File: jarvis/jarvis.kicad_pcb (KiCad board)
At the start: 4 copper layers, 17.5 x 45.8 mm, 30 parts, among them IC1 ESP32-S3R16V, IC2 MAX98357AETE+T, IC3 MCP73871T-4CAI_ML, IC4 TLV70033DDCT, J1 Conn_01x02 - Speaker, J2 Mic Conn_01x05, J3 Conn_01x02 - Battery, U1 W25Q64JVSSIQ, U2 2137160001, Y1 Crystal 32.768khz, Y2 Crystal 40mhz

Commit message: flash routed
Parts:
- removed PESD5: PESD5V0X1UAB,115, jarvis:PESD5V0X1UAB115
- removed U1: W25Q64JVSSIQ, jarvis:W25Q64JVSSIQ
- added AE1: RFANT3216120A5T, jarvis:ANT_RFANT3216120A5T_WAL, F.Cu at (146.1, 92.9)
- added C11: 0.1uf, Capacitor_SMD:C_0603_1608Metric, F.Cu at (72.5, 48.4)
- added C12: 0.1uf, Capacitor_SMD:C_0603_1608Metric, F.Cu at (72.5, 51.0)
- added C13: 0.1uf, Capacitor_SMD:C_0603_1608Metric, F.Cu at (76.5, 43.4)
- added C14: 12pf, Capacitor_SMD:C_0402_1005Metric, F.Cu at (82.0, 57.1)
- added C15: 0.1uf, Capacitor_SMD:C_0603_1608Metric, F.Cu at (76.5, 45.9)
- added C16: 12pf, Capacitor_SMD:C_0402_1005Metric, F.Cu at (82.0, 59.1)
- added C17: 1uf, Capacitor_SMD:C_0603_1608Metric, F.Cu at (76.5, 48.4)
- added C18: 0.1uf, Capacitor_SMD:C_0402_1005Metric, F.Cu at (82.0, 61.1)
- added C19: 0.1uf, Capacitor_SMD:C_0603_1608Metric, F.Cu at (76.5, 51.0)
- added C20: 10uf, Capacitor_SMD:C_0603_1608Metric, F.Cu at (80.6, 43.4)
- added C21: 1uf, Capacitor_SMD:C_0603_1608Metric, F.Cu at (80.6, 45.9)
- added IC5: W25Q128JWSIQ, jarvis:W25Q128JWSIQ-1.8, F.Cu at (165.7, 111.7)
- added L2: 24nh, jarvis:MLG1005SR24JT000, F.Cu at (75.9, 60.7)
- added L3: 6.8 nH, Inductor_SMD:L_01005_0402Metric, F.Cu at (147.8, 97.9)
- added PESD1: PESD5V0X1UAB,115, jarvis:PESD5V0X1UAB115, F.Cu at (62.8, 60.3)
- added R10: 0, Resistor_SMD:R_0603_1608Metric, F.Cu at (156.8, 112.4)
- added R11: 0, Resistor_SMD:R_0603_1608Metric, F.Cu at (156.8, 110.9)
- added R12: 0, Resistor_SMD:R_0603_1608Metric, F.Cu at (156.8, 109.3)
- added R13: 0, Resistor_SMD:R_0603_1608Metric, F.Cu at (156.8, 107.8)
- added R14: 0, Resistor_SMD:R_0603_1608Metric, F.Cu at (156.8, 113.9)
- added R15: 0, Resistor_SMD:R_0603_1608Metric, F.Cu at (156.8, 115.5)
- added R8: 10k, Resistor_SMD:R_0603_1608Metric, F.Cu at (80.6, 51.0)
- added R9: 10k, Resistor_SMD:R_0603_1608Metric, F.Cu at (153.8, 100.6)
- added S1: EVQ-P9H02W, jarvis:EVQP9H02W, F.Cu at (87.4, 57.1)
- C1: value 1uf -> 10uf
- C10, C9: footprint Capacitor_SMD:C_0603_1608Metric -> Capacitor_SMD:C_0402_1005Metric
- C2: value 10uf -> 4.7uf
- C3: value 4.7uf -> 1uf
- C7, C8: value 12pf -> 0.1uf
- IC1, IC2, IC3: moved to F.Cu
- R1: value 2k -> 10k
- R2: value 10k -> 2k
- R4: value 5.1k -> 22
- R6: value 22 -> 5.1k
- moved U2 120.3 mm to (53.7, 45.2), turned to 0 degrees
- moved R3 118.0 mm to (58.8, 55.3), turned to 0 degrees
- moved R4 114.8 mm to (58.8, 57.8), turned to 0 degrees
- moved C3 106.2 mm to (50.8, 60.4), turned to 0 degrees
- moved IC3 105.0 mm to (65.6, 45.1), turned to 0 degrees
- moved C1 104.7 mm to (50.8, 55.3), turned to 0 degrees
- moved C5 103.5 mm to (54.8, 55.3), turned to 0 degrees
- moved R2 102.8 mm to (54.8, 62.9), turned to 0 degrees
- moved R7 101.5 mm to (80.6, 48.4), turned to 0 degrees
- moved IC4 101.4 mm to (65.0, 50.1)
- moved J3 101.3 mm to (63.4, 57.1)
- moved C4 100.8 mm to (50.8, 62.9), turned to 0 degrees
- moved C2 100.6 mm to (50.8, 57.8), turned to 0 degrees
- moved C9 99.8 mm to (82.0, 53.2)
- moved C6 99.6 mm to (54.8, 57.8), turned to 0 degrees
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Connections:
- net Net-(IC1-GPIO18) renamed /ESP/ESP-GPIO17
- net Net-(IC1-GPIO3) renamed /Components/AMP-DIN
- C1 pad 1: VBUS -> /Power/VBAT_1
- C10 pad 1: Net-(IC1-XTAL_32K_P) -> Net-(IC1-XTAL_32K_N)
- C2 pad 1: /VBAT_1 -> GND
- C2 pad 2: GND -> /Power/SYS
- C3 pad 1: GND -> VBUS
- C3 pad 2: /SYS -> GND
- C4 pad 2: /SYS -> /Power/SYS
- C7 pad 1: Net-(IC1-XTAL_N) -> +3.3V
- C8 pad 1: GND -> +3.3V
- C8 pad 2: Net-(C8-Pad2) -> GND
- C9 pad 1: Net-(IC1-XTAL_32K_N) -> Net-(IC1-XTAL_32K_P)
- IC1 pad 1: unconnected-(IC1-LNA_IN-Pad1) -> Net-(IC1-LNA_IN)
- IC1 pad 10: Net-(IC1-GPIO5) -> /Components/AMP-BCLK
- IC1 pad 12: unconnected-(IC1-GPIO7-Pad12) -> /Components/MIC-WS
- IC1 pad 13: unconnected-(IC1-GPIO8-Pad13) -> /Components/MIC-BCK
- IC1 pad 14: unconnected-(IC1-GPIO9-Pad14) -> /Components/MIC-DATA
- IC1 pad 2: unconnected-(IC1-VDD3P3_1-Pad2) -> Net-(IC1-VDD3P3_1)
- IC1 pad 20: unconnected-(IC1-VDD3P3_RTC-Pad20) -> +3.3V
- IC1 pad 23: Net-(IC1-GPIO17) -> /ESP/ESP-GPIO18
- IC1 pad 25: Net-(IC1-GPIO19) -> /ESP/ESP-GPIO19
- IC1 pad 26: Net-(IC1-GPIO20) -> /ESP/ESP-GPIO20
- IC1 pad 27: Net-(IC1-GPIO21) -> /ESP/ESP-GPIO21
- IC1 pad 29: unconnected-(IC1-VDD_SPI-Pad29) -> +1.8
- IC1 pad 3: unconnected-(IC1-VDD3P3_2-Pad3) -> Net-(IC1-VDD3P3_1)
- IC1 pad 30: unconnected-(IC1-SPIHD-Pad30) -> Net-(IC1-SPIHD)
- IC1 pad 31: unconnected-(IC1-SPIWP-Pad31) -> Net-(IC1-SPIWP)
- IC1 pad 32: /SYS -> Net-(IC1-SPICS0)
- IC1 pad 4: unconnected-(IC1-CHIP_PU-Pad4) -> Net-(IC1-CHIP_PU)
- IC1 pad 43: Net-(IC1-GPIO38) -> unconnected-(IC1-GPIO38-Pad43)
- IC1 pad 46: unconnected-(IC1-VDD3P3_CPU-Pad46) -> +3.3V
- IC1 pad 52: Net-(IC1-GPIO46) -> unconnected-(IC1-GPIO46-Pad52)
- IC1 pad 55: unconnected-(IC1-VDDA_1-Pad55) -> +3.3V
- IC1 pad 56: unconnected-(IC1-VDDA_2-Pad56) -> +3.3V
- IC1 pad 9: Net-(IC1-GPIO4) -> /Components/AMP-LRCLK
- IC2 pad 14: Net-(IC1-GPIO5) -> /Components/AMP-LRCLK
- IC2 pad 16: Net-(IC1-GPIO4) -> /Components/AMP-BCLK
- IC2 pad 4: +3.3V -> /Components/+3.3V
- IC2 pad 7: +3.3V -> /Components/+3.3V
- IC2 pad 8: +3.3V -> /Components/+3.3V
- IC3 pad 1: /SYS -> /Power/SYS
- IC3 pad 13: /PROG1 -> /Power/PROG1
- IC3 pad 14: /VBAT_1 -> /Power/VBAT_1
- IC3 pad 17: /VBAT_1 -> /Power/VBAT_1
- IC3 pad 20: /SYS -> /Power/SYS
- IC3 pad 5: /THERM -> /Power/THERM
- IC3 pad 7: Net-(IC1-GPIO17) -> /ESP/ESP-GPIO21
- IC3 pad 8: Net-(IC1-GPIO21) -> /ESP/ESP-GPIO18
- IC4 pad 1: /SYS -> /Power/SYS
- IC4 pad 3: /SYS -> /Power/SYS
- J2 pad 1: Net-(IC1-GPIO38) -> /Components/MIC-DATA
- J2 pad 2: Net-(IC1-GPIO45) -> /Components/MIC-WS
- J2 pad 3: Net-(IC1-GPIO46) -> /Components/MIC-BCK
- J2 pad 4: +3.3V -> /Components/+3.3
- J3 pad 1: /VBAT_1 -> /Power/VBAT_1
- L1 pad 2: Net-(C8-Pad2) -> Net-(C14-Pad2)
- R1 pad 1: /PROG1 -> GND
- R1 pad 2: GND -> /Power/THERM
- R2 pad 1: GND -> /Power/PROG1
- R2 pad 2: /THERM -> GND
- R4 pad 1: GND -> /Power/USB_DP
- R4 pad 2: Net-(U2-CC2) -> /ESP/ESP-GPIO19
- R5 pad 1: /USB_DP -> /Power/USB_DN
- R5 pad 2: Net-(IC1-GPIO19) -> /ESP/ESP-GPIO20
- R6 pad 1: /USB_DN -> GND
- R6 pad 2: Net-(IC1-GPIO20) -> Net-(U2-CC2)
- U2 pad A6: /USB_DP -> /Power/USB_DP
- U2 pad A7: /USB_DN -> /Power/USB_DN
- U2 pad B6: /USB_DP -> /Power/USB_DP
- U2 pad B7: /USB_DN -> /Power/USB_DN
- Y2 pad 2: Net-(C8-Pad2) -> Net-(C14-Pad2)
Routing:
- net GND: track 64.2 -> 1.60 mm, vias 20 -> 1
- net /USB_DN: track 47.8 -> 0.00 mm, vias 1 -> 0
- net /SYS: track 40.2 -> 0.00 mm, vias 2 -> 0
- net VBUS: track 37.4 -> 0.00 mm, vias 3 -> 0
- net +3.3V: track 30.1 -> 0.00 mm, vias 3 -> 0
- net Net-(IC1-XTAL_32K_P): track 27.8 -> 0.00 mm, vias 1 -> 0
- net Net-(IC1-XTAL_32K_N): track 27.6 -> 0.00 mm, vias 1 -> 0
- net Net-(U2-CC2): track 21.6 -> 0.00 mm, vias 1 -> 0
- net Net-(IC1-GPIO17): track 20.4 -> 0.00 mm
- net Net-(IC1-GPIO21): track 19.4 -> 0.00 mm
- net +1.8: track 0.00 -> 19.3 mm, vias 0 -> 2
- net /ESP/ESP-GPIO17: track 18.8 -> 0.00 mm
- net Net-(IC1-GPIO46): track 18.0 -> 0.00 mm
- net /VBAT_1: track 17.3 -> 0.00 mm, vias 1 -> 0
- net Net-(IC1-GPIO45): track 16.4 -> 0.00 mm
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- removed copper zone on In2.Cu, net +3.3V
- removed copper zone on In1.Cu, net GND
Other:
- board outline removed
- board text removed: "Jarvis"

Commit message: start crystal layout
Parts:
- moved IC4 141.1 mm to (184.3, 125.3)
- moved J3 133.2 mm to (169.9, 137.2)
- moved IC3 125.4 mm to (151.7, 136.2)
- moved U2 125.0 mm to (173.6, 80.4)
- moved Y1 96.7 mm to (148.1, 119.2)
- moved J2 94.4 mm to (117.2, 138.7)
- moved Y2 86.7 mm to (149.0, 102.8), turned to 180 degrees
- moved L1 86.1 mm to (148.2, 105.2), turned to 90 degrees
- moved C16 81.3 mm to (151.1, 102.0), turned to 90 degrees
- moved C14 78.5 mm to (146.7, 101.7), turned to -90 degrees
- moved IC2 65.5 mm to (124.0, 122.8)
- moved J1 65.5 mm to (117.6, 123.5)
- moved S1 62.2 mm to (119.6, 110.2)
- moved C8 54.6 mm to (114.8, 80.4)
- moved R1 54.6 mm to (97.1, 94.8)
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
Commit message: crystals done
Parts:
- removed Y1: Crystal 32.768khz, jarvis:XTAL_CM8V-T1A-32.768KHZ-7PF-20PPM-TA-QC
- added Y3: ECS-.327-12.5-1210B-N-TR, jarvis:XTAL_ECS-.327-12.5-1210B-N-TR, F.Cu at (149.0, 120.8)
- C10, C9: value 12pf -> 12.5pf
- Y2: value Crystal 40mhz -> ABM10W-40.0000MHZ-8-N1G-T3; footprint jarvis:XTAL_CM8V-T1A-32.768KHZ-7PF-20PPM-TA-QC -> jarvis:XTAL_ABM10W-40.0000MHZ-8-N1G-T3
- moved C1 101.4 mm to (179.9, 142.1)
- moved R3 84.5 mm to (164.5, 145.8)
- moved R4 84.1 mm to (169.0, 142.0)
- moved R2 78.4 mm to (171.7, 121.5)
- moved R6 77.1 mm to (163.9, 142.1)
- moved R5 75.5 mm to (159.7, 142.4)
- moved C3 75.4 mm to (153.4, 140.0)
- moved R1 70.4 mm to (160.4, 125.6)
- moved C5 69.2 mm to (147.6, 137.2)
- moved C2 68.8 mm to (149.5, 131.6)
- moved C4 67.5 mm to (149.5, 134.3)
- moved C6 63.7 mm to (149.4, 128.8)
- moved U2 50.9 mm to (159.7, 129.4)
- moved C17 49.4 mm to (154.6, 117.0), turned to 90 degrees
- moved R7 47.7 mm to (149.1, 122.7)
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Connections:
- IC2 pad 4: /Components/+3.3V -> +3.3V
- IC2 pad 7: /Components/+3.3V -> +3.3V
- IC2 pad 8: /Components/+3.3V -> +3.3V
- J2 pad 4: /Components/+3.3 -> +3.3V
- Y2 pad 1: Net-(IC1-XTAL_N) -> Net-(C14-Pad2)
- Y2 pad 2: Net-(C14-Pad2) -> GND
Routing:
- net GND: track 1.60 -> 24.3 mm, vias 1 -> 8
- net /Components/MIC-WS: track 0.00 -> 20.5 mm
- net /Components/MIC-DATA: track 0.00 -> 16.1 mm
- net Net-(IC1-CHIP_PU): track 0.00 -> 15.1 mm
- net /Components/MIC-BCK: track 0.00 -> 14.7 mm
- net Net-(IC1-XTAL_32K_N): track 0.00 -> 13.8 mm
- net Net-(IC1-XTAL_N): track 0.00 -> 13.5 mm
- net Net-(IC1-XTAL_32K_P): track 0.00 -> 11.9 mm
- net /Components/AMP-DIN: track 0.00 -> 11.8 mm
- net +3.3V: track 0.00 -> 11.8 mm, vias 0 -> 5
- net /Components/AMP-BCLK: track 0.00 -> 11.5 mm, vias 0 -> 2
- net /Components/AMP-LRCLK: track 0.00 -> 10.6 mm
- net Net-(IC1-GPIO45): track 0.00 -> 8.32 mm
- net Net-(IC2-OUTP): track 0.00 -> 5.44 mm
- net Net-(C14-Pad2): track 0.00 -> 4.29 mm
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- added copper zone on In2.Cu, net +3.3V
- added copper zone on In1.Cu, net GND

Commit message: initial all connections
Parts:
- moved PESD1 71.0 mm to (167.3, 129.1)
- moved C13 42.0 mm to (142.7, 112.5)
- moved C7 41.3 mm to (145.2, 105.8), turned to -90 degrees
- moved C20 41.2 mm to (142.7, 114.0)
- moved C8 38.5 mm to (143.7, 105.8), turned to -90 degrees
- moved L2 38.4 mm to (143.2, 109.7)
- moved C12 37.8 mm to (142.7, 111.0)
- moved C11 37.8 mm to (142.7, 108.4), turned to 180 degrees
- moved C1 32.7 mm to (149.9, 129.1), turned to 180 degrees
- moved C21 26.8 mm to (134.9, 104.3), turned to 180 degrees
- moved R6 25.3 mm to (161.2, 117.0)
- moved J3 25.1 mm to (145.9, 128.6), turned to 180 degrees
- moved R8 23.8 mm to (134.9, 105.9)
- moved R2 22.6 mm to (150.0, 127.5), turned to 180 degrees
- moved R5 21.0 mm to (158.1, 121.5), turned to 90 degrees
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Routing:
- net GND: track 24.3 -> 58.8 mm, vias 8 -> 17
- net VBUS: track 0.00 -> 25.4 mm, vias 0 -> 3
- net +3.3V: track 11.8 -> 34.8 mm, vias 5 -> 7
- net /ESP/ESP-GPIO18: track 0.00 -> 20.1 mm, vias 0 -> 2
- net /ESP/ESP-GPIO21: track 0.00 -> 18.4 mm, vias 0 -> 2
- net /ESP/ESP-GPIO19: track 0.00 -> 16.6 mm, vias 0 -> 2
- net /ESP/ESP-GPIO17: track 0.00 -> 15.4 mm, vias 0 -> 2
- net Net-(IC1-LNA_IN): track 0.00 -> 13.6 mm, vias 0 -> 2
- net /Power/VBAT_1: track 0.00 -> 13.1 mm
- net Net-(U2-CC1): track 0.00 -> 12.2 mm, vias 0 -> 1
- net /ESP/ESP-GPIO20: track 0.00 -> 11.3 mm, vias 0 -> 2
- net /Power/SYS: track 0.00 -> 8.55 mm, vias 0 -> 2
- net Net-(IC1-CHIP_PU): track 15.1 -> 21.7 mm, vias 0 -> 2
- net /Components/AMP-LRCLK: track 10.6 -> 16.9 mm, vias 0 -> 2
- net Net-(U2-CC2): track 0.00 -> 5.95 mm
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- added copper zone on In2.Cu, net /Power/SYS
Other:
- board outline added: 36.6 x 35.3 mm

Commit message: details
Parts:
- moved C15 0.41 mm to (148.0, 116.0)
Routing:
- net GND: track 58.8 -> 69.0 mm, vias 17 -> 24
- net +3.3V: track 34.8 -> 36.6 mm
- net /ESP/ESP-GPIO21: track 18.4 -> 17.1 mm
- net /ESP/ESP-GPIO19: track 16.6 -> 17.8 mm
- net /ESP/ESP-GPIO20: track 11.3 -> 12.4 mm
- net /ESP/ESP-GPIO17: track 15.4 -> 16.1 mm
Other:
- board size 36.6 x 35.3 mm -> 37.1 x 35.8 mm

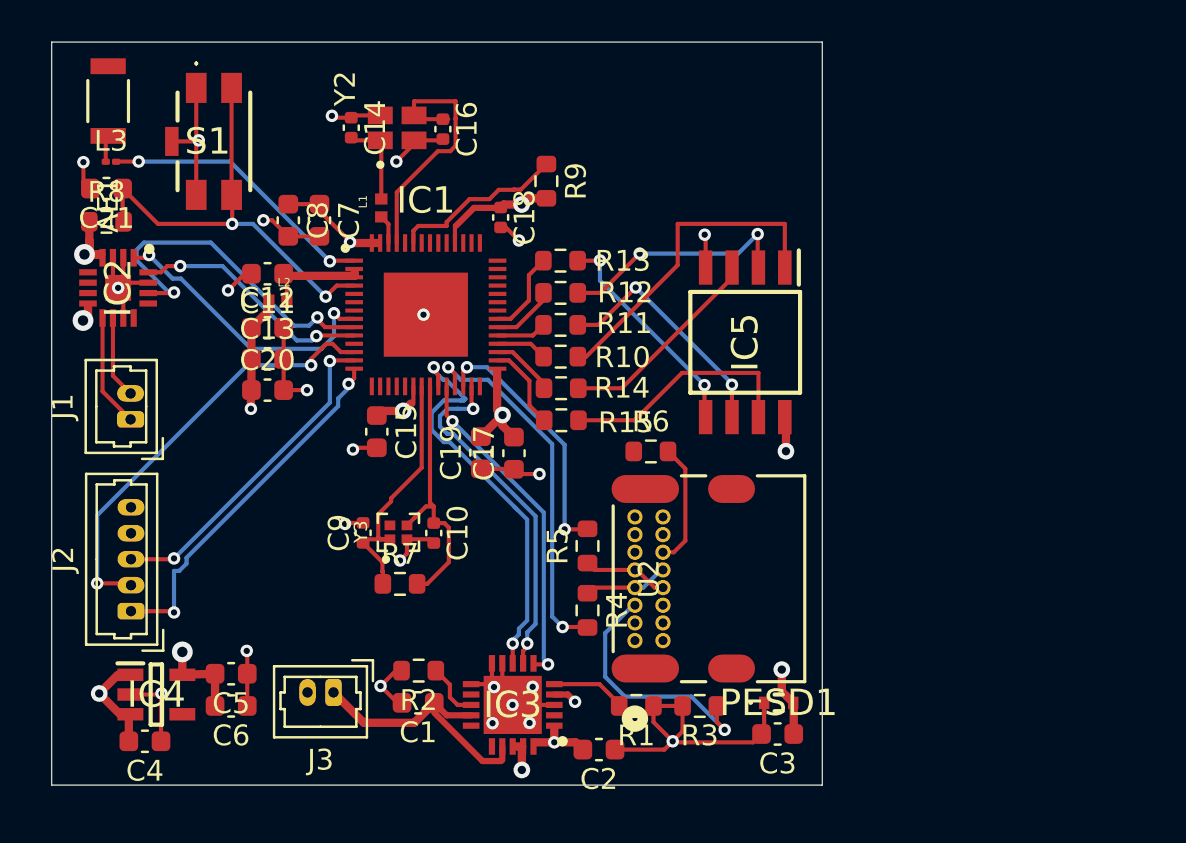
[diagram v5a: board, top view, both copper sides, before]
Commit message: with leds and boot button
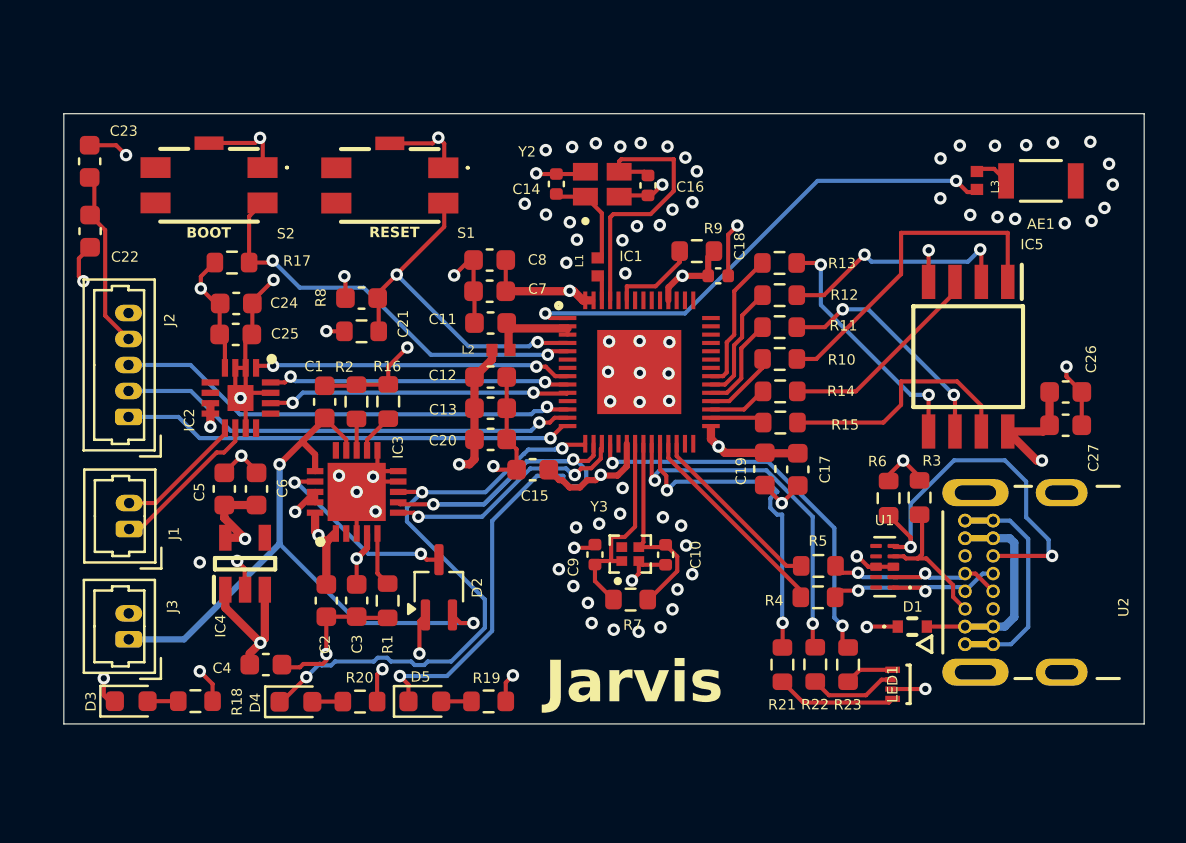
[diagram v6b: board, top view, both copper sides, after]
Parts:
- removed PESD1: PESD5V0X1UAB,115, jarvis:PESD5V0X1UAB115
- added C22: 100nf, Capacitor_SMD:C_0603_1608Metric, F.Cu at (134.2, 106.3)
- added C23: 1uf, Capacitor_SMD:C_0603_1608Metric, F.Cu at (134.1, 103.0)
- added C24: 0.1uf, Capacitor_SMD:C_0603_1608Metric, F.Cu at (141.2, 111.3)
- added C25: 10uf, Capacitor_SMD:C_0603_1608Metric, F.Cu at (141.2, 109.8)
- added C26: 0.1uf, Capacitor_SMD:C_0603_1608Metric, F.Cu at (181.1, 114.1)
- added C27: 10uf, Capacitor_SMD:C_0603_1608Metric, F.Cu at (181.1, 115.7)
- added D1: PESD5V0X1UAB,115, jarvis:PESD5V0X1UAB115, F.Cu at (173.7, 125.4)
- added D2: BAT54CW, Package_TO_SOT_SMD:SOT-323_SC-70_Handsoldering, F.Cu at (150.9, 123.5)
- added D3: LED, LED_SMD:LED_0603_1608Metric, F.Cu at (136.1, 129.0)
- added D4: LED, LED_SMD:LED_0603_1608Metric, F.Cu at (144.1, 129.0)
- added D5: LED, LED_SMD:LED_0603_1608Metric, F.Cu at (150.3, 129.0)
- added LED1: IN-S63TBS5R5G5B, jarvis:IN-S63TBS5R5G5B_INO, F.Cu at (173.1, 128.2)
- added R16: 2k, Resistor_SMD:R_0603_1608Metric, F.Cu at (148.5, 114.5)
- added R17: 10k, Resistor_SMD:R_0603_1608Metric, F.Cu at (141.0, 107.9)
- added R18: 560, Resistor_SMD:R_0603_1608Metric, F.Cu at (139.2, 129.0)
- added R19: 560, Resistor_SMD:R_0603_1608Metric, F.Cu at (153.3, 129.0)
- added R20: 560, Resistor_SMD:R_0603_1608Metric, F.Cu at (147.2, 129.0)
- added R21: 330, Resistor_SMD:R_0603_1608Metric, F.Cu at (167.5, 127.2)
- added R22: 330, Resistor_SMD:R_0603_1608Metric, F.Cu at (169.1, 127.2)
- added R23: 330, Resistor_SMD:R_0603_1608Metric, F.Cu at (170.6, 127.2)
- added S2: EVQ-P9H02W Boot, jarvis:EVQP9H02W, F.Cu at (139.9, 104.1)
- added U1: TPD4E05U06QDQARQ1, jarvis:IC_TPD4E05U06QDQARQ1, F.Cu at (172.4, 122.5)
- L3: footprint Inductor_SMD:L_01005_0402Metric -> jarvis:MLG1005SR24JT000
- U2: footprint jarvis:2137160001_MOL -> jarvis:MOLEX_2137160001-holes
- moved AE1 45.1 mm to (179.9, 103.9), turned to 0 degrees
- moved L3 41.7 mm to (176.8, 103.9), turned to -90 degrees
- moved U2 23.7 mm to (183.9, 123.3)
- moved C3 21.3 mm to (147.0, 124.1), turned to -90 degrees
- moved C1 15.2 mm to (145.4, 114.6), turned to 90 degrees
- moved C2 15.0 mm to (145.5, 124.1), turned to 90 degrees
- moved R3 14.6 mm to (174.1, 119.2), turned to 90 degrees
- moved C17 13.7 mm to (168.2, 117.8)
- moved C19 13.7 mm to (166.6, 117.8)
- moved C21 13.4 mm to (147.2, 109.6)
- moved R8 13.4 mm to (147.2, 111.2)
- moved R2 13.3 mm to (147.0, 114.6), turned to 90 degrees
- moved R1 13.0 mm to (148.5, 124.1), turned to 90 degrees
- moved IC3 12.7 mm to (147.0, 118.9), turned to 90 degrees
- moved R6 11.7 mm to (172.6, 119.2), turned to -90 degrees
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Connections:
- C3 pad 1: VBUS -> /Power/VBUS
- IC1 pad 10: /Components/AMP-BCLK -> /Components/AMP-LRCLK
- IC1 pad 12: /Components/MIC-WS -> /Components/MIC-BCK
- IC1 pad 13: /Components/MIC-BCK -> /Components/MIC-WS
- IC1 pad 15: unconnected-(IC1-GPIO10-Pad15) -> /ESP/ESP-GPIO10
- IC1 pad 16: unconnected-(IC1-GPIO11-Pad16) -> /ESP/ESP-GPIO11
- IC1 pad 17: unconnected-(IC1-GPIO12-Pad17) -> /ESP/ESP-GPIO12
- IC1 pad 18: unconnected-(IC1-GPIO13-Pad18) -> Net-(IC1-GPIO13)
- IC1 pad 23: /ESP/ESP-GPIO18 -> Net-(IC1-GPIO17)
- IC1 pad 24: /ESP/ESP-GPIO17 -> Net-(IC1-GPIO18)
- IC1 pad 5: unconnected-(IC1-GPIO0-Pad5) -> Net-(IC1-GPIO0)
- IC1 pad 9: /Components/AMP-LRCLK -> /Components/AMP-BCLK
- IC3 pad 12: unconnected-(IC3-PROG3-Pad12) -> Net-(IC3-PROG3)
- IC3 pad 15: unconnected-(IC3-VBAT_2-Pad15) -> /Power/VBAT_1
- IC3 pad 16: unconnected-(IC3-VBAT_SENSE-Pad16) -> /Power/VBAT_1
- IC3 pad 17: /Power/VBAT_1 -> Net-(IC3-CE)
- IC3 pad 18: VBUS -> /Power/VBUS
- IC3 pad 19: VBUS -> /Power/VBUS
- IC3 pad 4: VBUS -> /Power/VBUS
- IC3 pad 6: /ESP/ESP-GPIO17 -> /ESP/ESP-GPIO12
- IC3 pad 7: /ESP/ESP-GPIO21 -> /ESP/ESP-GPIO11
- IC3 pad 8: /ESP/ESP-GPIO18 -> /ESP/ESP-GPIO10
- J1 pad 1: Net-(IC2-OUTP) -> Net-(IC2-OUTN)
- J1 pad 2: Net-(IC2-OUTN) -> Net-(IC2-OUTP)
- S1 pad 3: GND -> unconnected-(S1-NO_2-Pad3)
- S1 pad 4: Net-(IC1-CHIP_PU) -> unconnected-(S1-COM_2-Pad4)
- U2 pad A4: VBUS -> /Power/VBUS
- U2 pad A9: VBUS -> /Power/VBUS
- U2 pad B4: unconnected-(U2-VBUS-PadB4) -> /Power/VBUS
- U2 pad B9: VBUS -> /Power/VBUS
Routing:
- net /Power/VBUS: track 0.00 -> 55.0 mm, vias 0 -> 3
- net /ESP/ESP-GPIO11: track 0.00 -> 37.8 mm, vias 0 -> 3
- net +3.3V: track 36.6 -> 74.1 mm, vias 7 -> 12
- net /ESP/ESP-GPIO10: track 0.00 -> 30.1 mm, vias 0 -> 3
- net VBUS: track 25.6 -> 0.00 mm, vias 3 -> 0
- net GND: track 69.0 -> 92.4 mm, vias 24 -> 90
- net Net-(IC1-GPIO0): track 0.00 -> 20.5 mm, vias 0 -> 2
- net /ESP/ESP-GPIO18: track 19.8 -> 0.00 mm, vias 2 -> 0
- net Net-(IC1-GPIO13): track 0.00 -> 19.0 mm, vias 0 -> 2
- net /Power/VBAT_1: track 13.3 -> 31.9 mm, vias 0 -> 2
- net /ESP/ESP-GPIO21: track 17.1 -> 0.00 mm, vias 2 -> 0
- net Net-(IC1-GPIO17): track 0.00 -> 17.0 mm, vias 0 -> 2
- net Net-(IC1-GPIO18): track 0.00 -> 16.2 mm, vias 0 -> 2
- net /ESP/ESP-GPIO17: track 16.1 -> 0.00 mm, vias 2 -> 0
- net Net-(U2-CC2): track 5.95 -> 18.8 mm, vias 0 -> 2
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- removed copper zone on In2.Cu, net /Power/SYS
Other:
- board size 37.1 x 35.8 mm -> 52 x 29.4 mm
- board text added: "BOOT"
- board text added: "Jarvis"
- board text added: "RESET"
